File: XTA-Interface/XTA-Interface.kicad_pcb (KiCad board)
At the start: 2 copper layers, 99.9 x 99.9 mm, 19 parts, among them CN1 DRIVE 0, CN2 DRIVE 1, CN3 LEDs, CN4 Drive Power, J3 Bus_ISA_8bit, U1 BIOS FLASH, U2 74HCT245, U3 ATF/GAL16V8-15 "LEFT", U4 ATF/GAL16V8-15 "RIGHT"

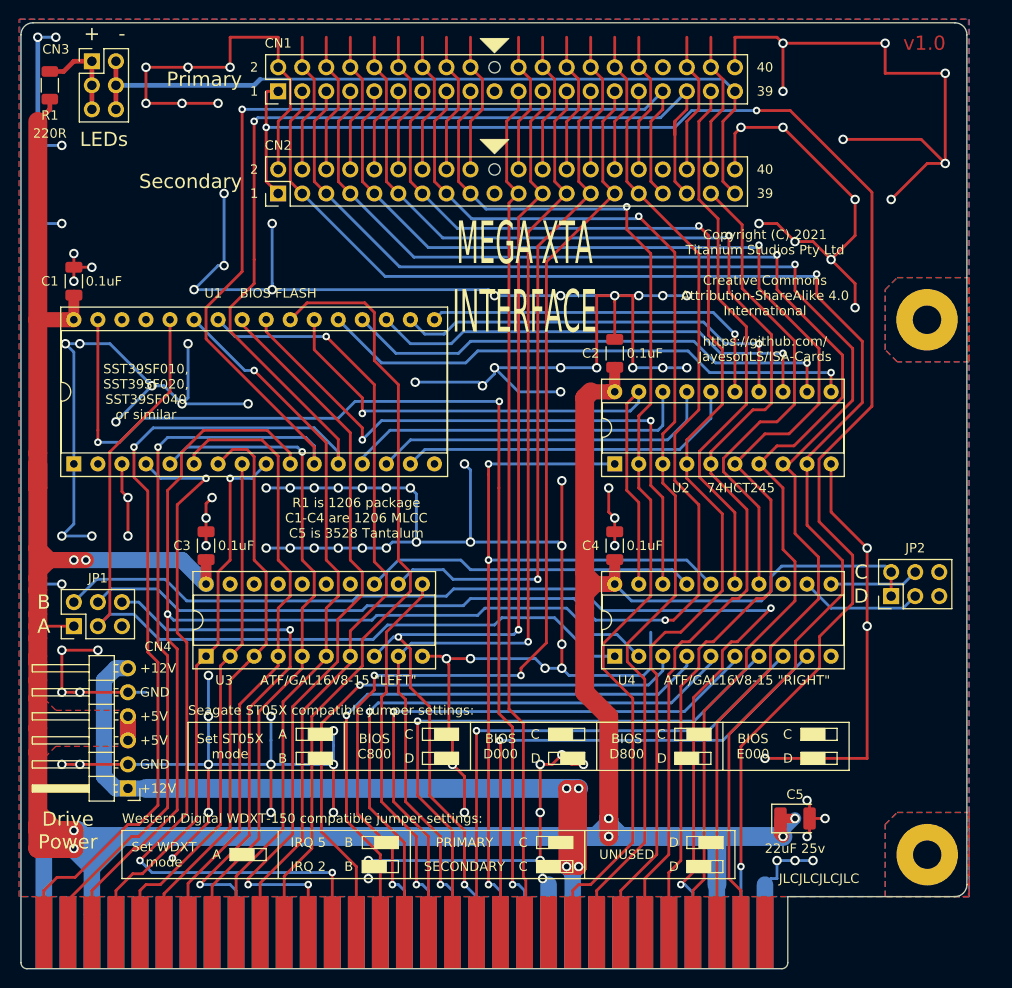
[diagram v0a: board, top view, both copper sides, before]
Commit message: Minor XTA interface tweaks.
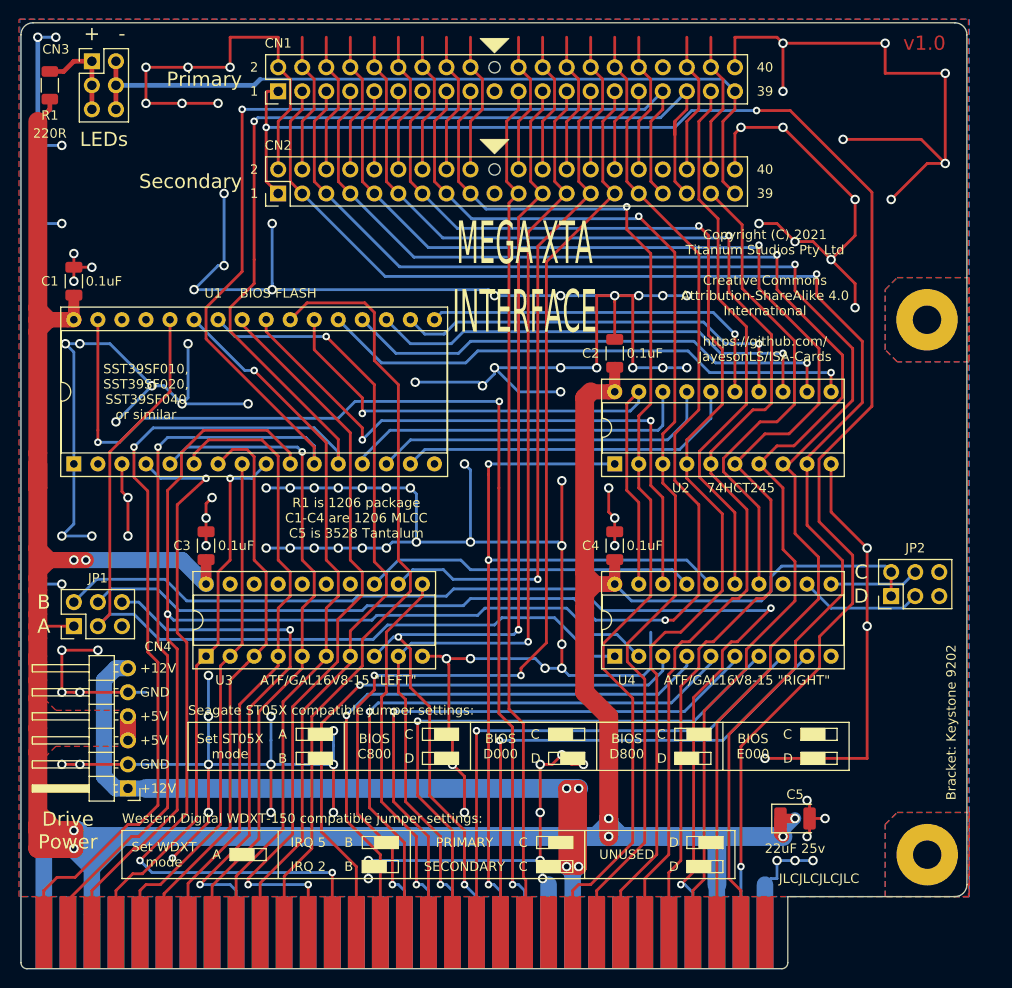
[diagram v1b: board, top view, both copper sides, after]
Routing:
- net VCC: track 367.6 -> 375.3 mm
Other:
- board text added: "Bracket: Keystone 9202"
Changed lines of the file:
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@@
   (general
     (thickness 1.6)
-    (drawings 167)
-    (tracks 1324)
+    (drawings 168)
+    (tracks 1333)
     (zones 0)
     (modules 19)
@@
     (pad 1 connect rect (at 0 0) (size 1.78 7.62) (layers B.Cu B.Mask)
       (net 28 GND))
+  )
+  (gr_text "Bracket: Keystone 9202" (at 194.945 116.205 90) (layer F.SilkS)
+    (effects (font (size 1 1) (thickness 0.15)))
   )
   (gr_text "Drive\nPower" (at 101.6 127.635) (layer F.SilkS)
@@
   (segment (start 98.806 101.854) (end 98.425 102.235) (width 0.3) (layer F.Cu) (net 29))
   (segment (start 98.425 87.757) (end 98.425 91.44) (width 2) (layer F.Cu) (net 29))
-  (segment (start 98.425 73.66) (end 98.425 87.757) (width 2) (layer F.Cu) (net 29))
   (segment (start 102.235 73.66) (end 98.425 73.66) (width 1.6) (layer F.Cu) (net 29))
   (via (at 158.75 128.27) (size 1) (drill 0.6) (layers F.Cu B.Cu) (net 29))
-  (segment (start 102.235 73.66) (end 102.235 71.071) (width 1.15) (layer F.Cu) (net 29))
   (segment (start 170.18 128.27) (end 177.165 128.27) (width 2) (layer B.Cu) (net 29))
   (via (at 177.165 128.27) (size 1) (drill 0.6) (layers F.Cu B.Cu) (net 29))
@@
   (segment (start 159.385 101.6) (end 161.163 103.378) (width 0.3) (layer B.Cu) (net 29))
   (segment (start 99.695 50.3575) (end 99.695 51.435) (width 0.5) (layer F.Cu) (net 29))
-  (segment (start 98.425 52.705) (end 98.425 73.66) (width 2) (layer F.Cu) (net 29))
   (segment (start 99.695 51.435) (end 98.425 52.705) (width 0.5) (layer F.Cu) (net 29))
   (segment (start 99.695 99.06) (end 98.425 97.79) (width 1.7) (layer F.Cu) (net 29))
@@
   (segment (start 98.425 97.79) (end 98.425 100.965) (width 2) (layer F.Cu) (net 29))
   (segment (start 98.425 100.965) (end 98.425 102.235) (width 2) (layer F.Cu) (net 29))
+  (segment (start 99.695 73.66) (end 98.425 72.39) (width 1.6) (layer F.Cu) (net 29))
+  (segment (start 98.425 72.39) (end 98.425 73.66) (width 2) (layer F.Cu) (net 29))
+  (segment (start 98.425 52.705) (end 98.425 72.39) (width 2) (layer F.Cu) (net 29))
+  (segment (start 99.695 73.66) (end 98.425 74.93) (width 1.6) (layer F.Cu) (net 29))
+  (segment (start 98.425 74.93) (end 98.425 87.757) (width 2) (layer F.Cu) (net 29))
+  (segment (start 98.425 73.66) (end 98.425 74.93) (width 2) (layer F.Cu) (net 29))
+  (segment (start 102.235 73.025) (end 101.6 73.66) (width 1.15) (layer F.Cu) (net 29))
+  (segment (start 101.6 73.66) (end 99.695 73.66) (width 1.6) (layer F.Cu) (net 29))
+  (segment (start 102.235 73.66) (end 101.6 73.66) (width 1.6) (layer F.Cu) (net 29))
+  (segment (start 102.235 72.39) (end 102.235 73.025) (width 1.15) (layer F.Cu) (net 29))
+  (segment (start 102.235 73.66) (end 102.235 72.39) (width 1.15) (layer F.Cu) (net 29))
+  (segment (start 102.235 72.39) (end 102.235 71.071) (width 1.15) (layer F.Cu) (net 29))
   (segment (start 154.305 51.435) (end 154.305 49.53) (width 0.3) (layer F.Cu) (net 30))
   (segment (start 153.044999 52.695001) (end 154.305 51.435) (width 0.3) (layer F.Cu) (net 30))

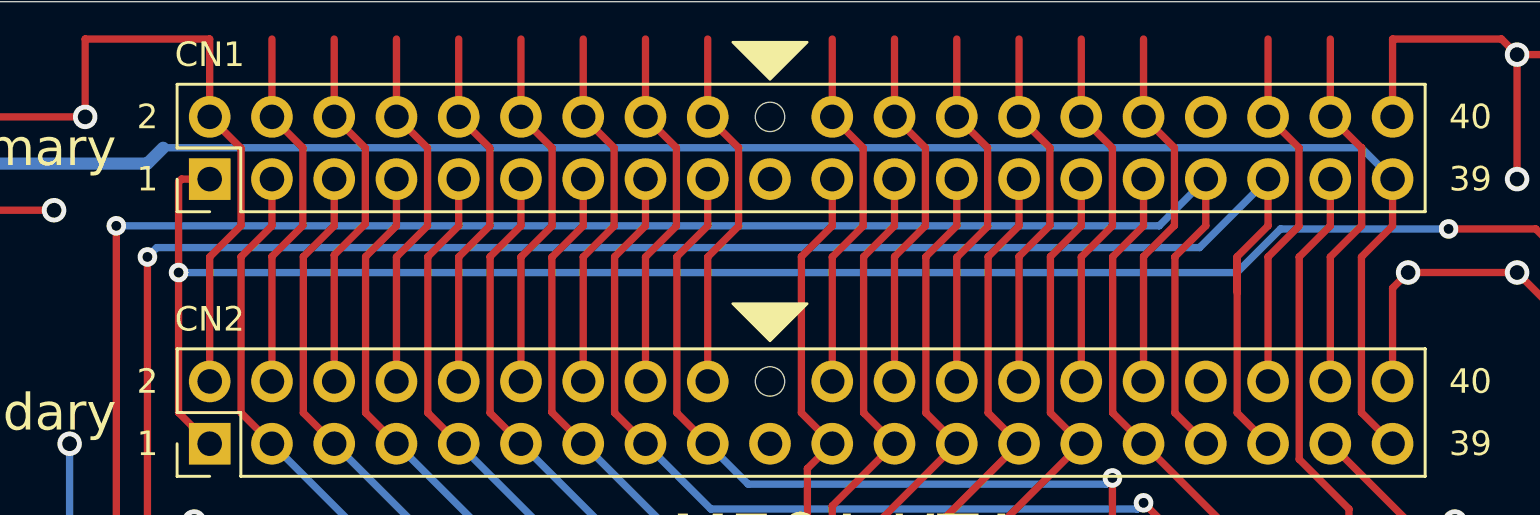
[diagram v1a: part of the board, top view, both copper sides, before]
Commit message: Add some caution messages to XTA interface.
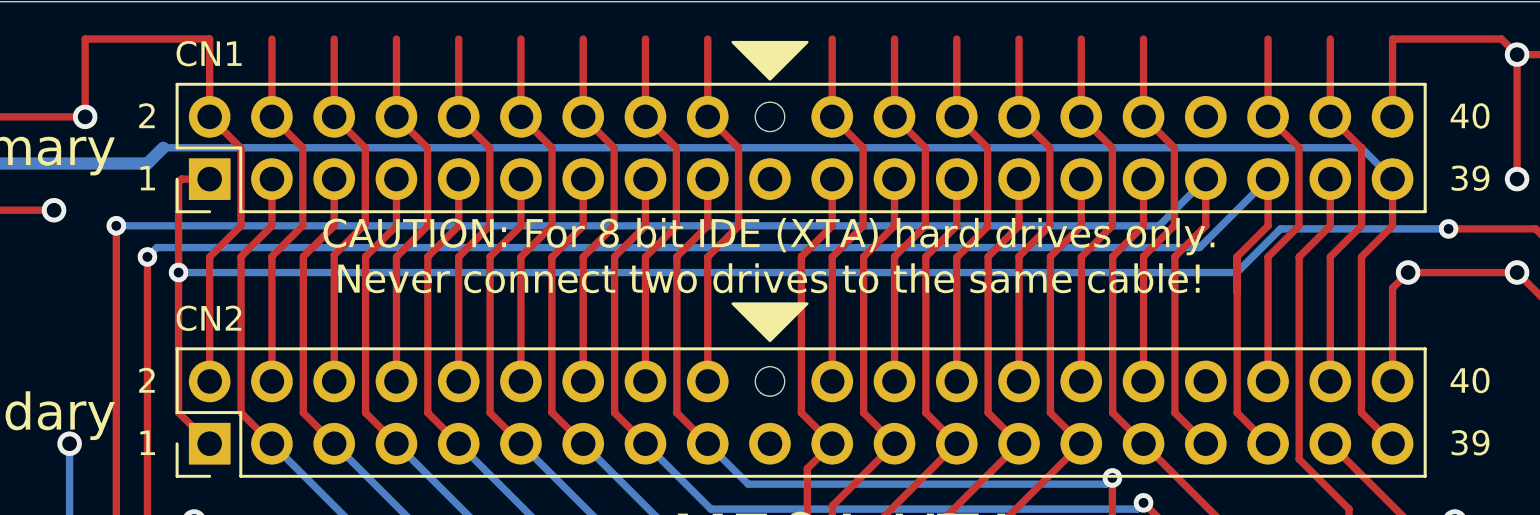
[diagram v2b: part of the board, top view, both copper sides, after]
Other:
- board text added: "CAUTION: For 8 bit IDE (XTA) hard drives only. Never connect two drives to the same cable!"

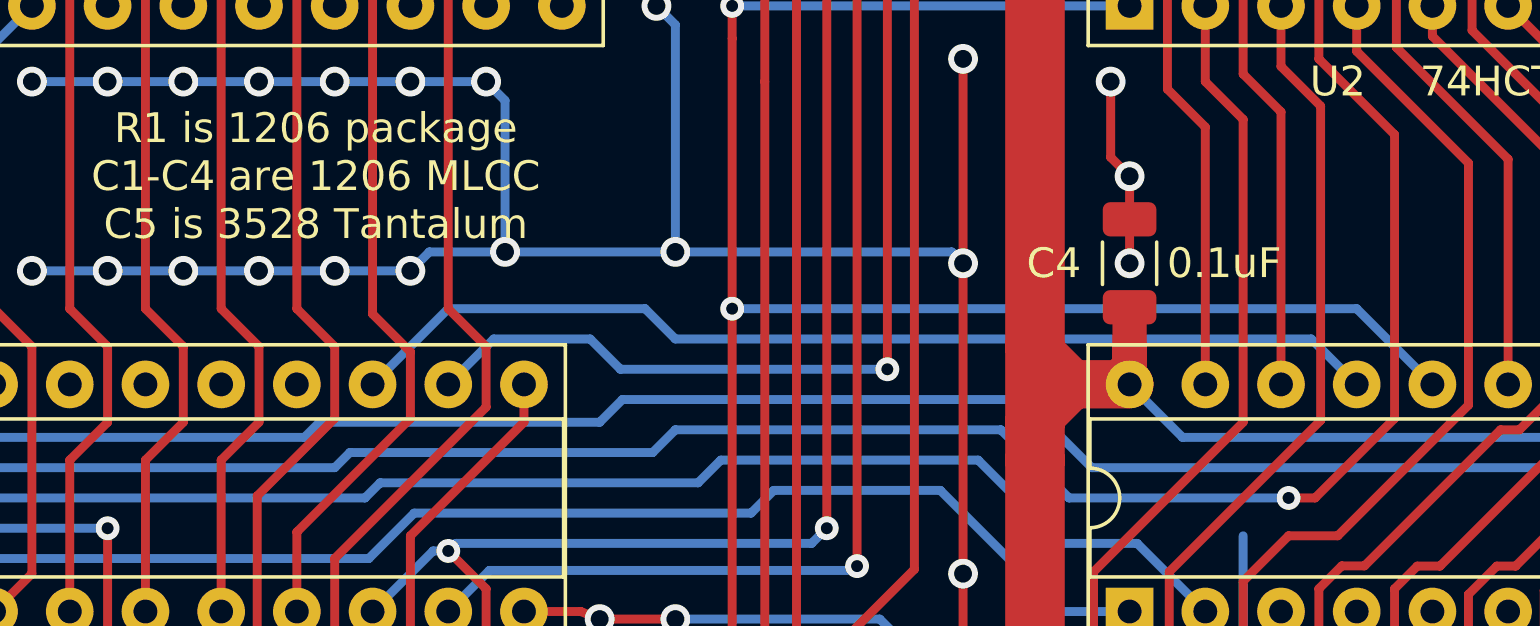
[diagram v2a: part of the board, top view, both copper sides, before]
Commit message: Add left GAL logic for XTA interface. Involved one pin swap to account for two of the 16V8 pins not having feedback.
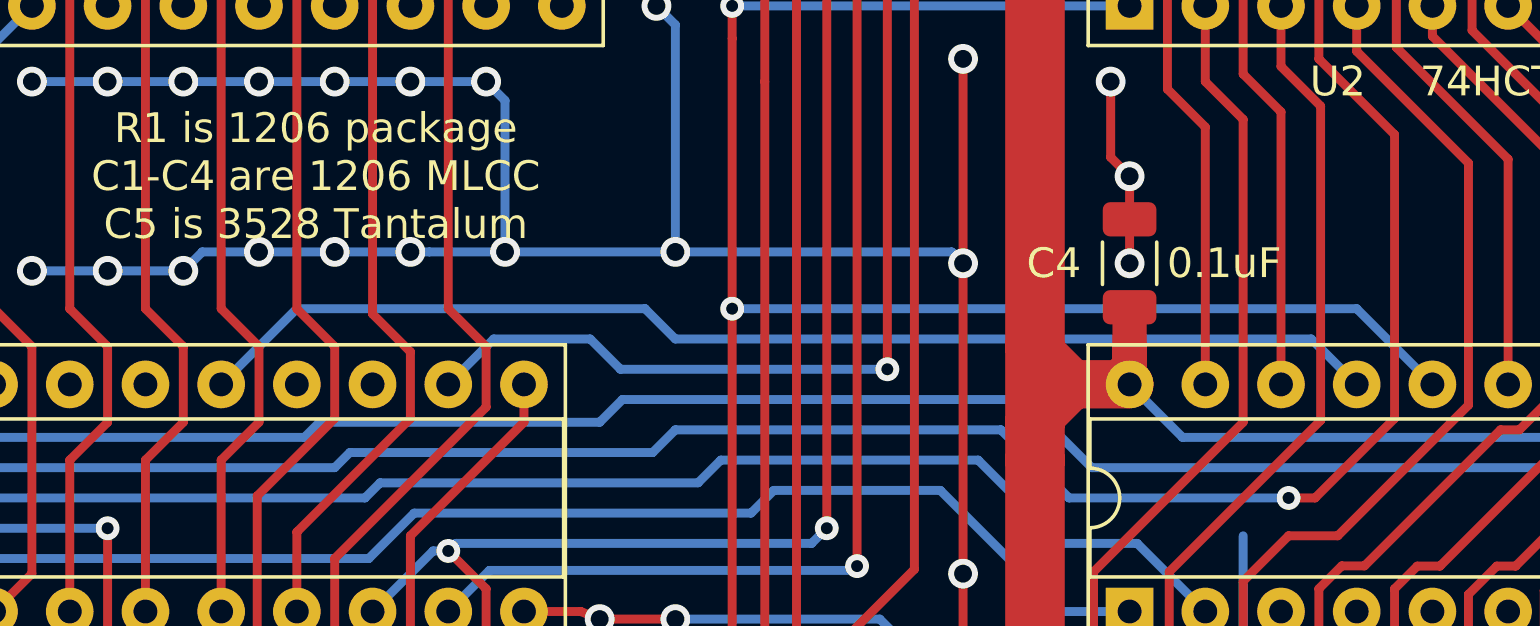
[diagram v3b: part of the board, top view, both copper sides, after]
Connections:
- net Net-(U3-Pad14) renamed /IOR_DELAY2
- net Net-(U3-Pad16) renamed /IOR_DELAY_DEBUG
- net Net-(U3-Pad17) renamed /IOR_DELAY3
- net Net-(U3-Pad18) renamed /IOR_DELAY4
- net Net-(U3-Pad19) renamed /IOR_DELAY5
- U3 pad 13: DECODE_IO_RANGE -> /IOR_DELAY1
- U3 pad 15: Net-(U3-Pad15) -> DECODE_IO_RANGE
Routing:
- net DECODE_IO_RANGE: track 35.1 -> 40.2 mm

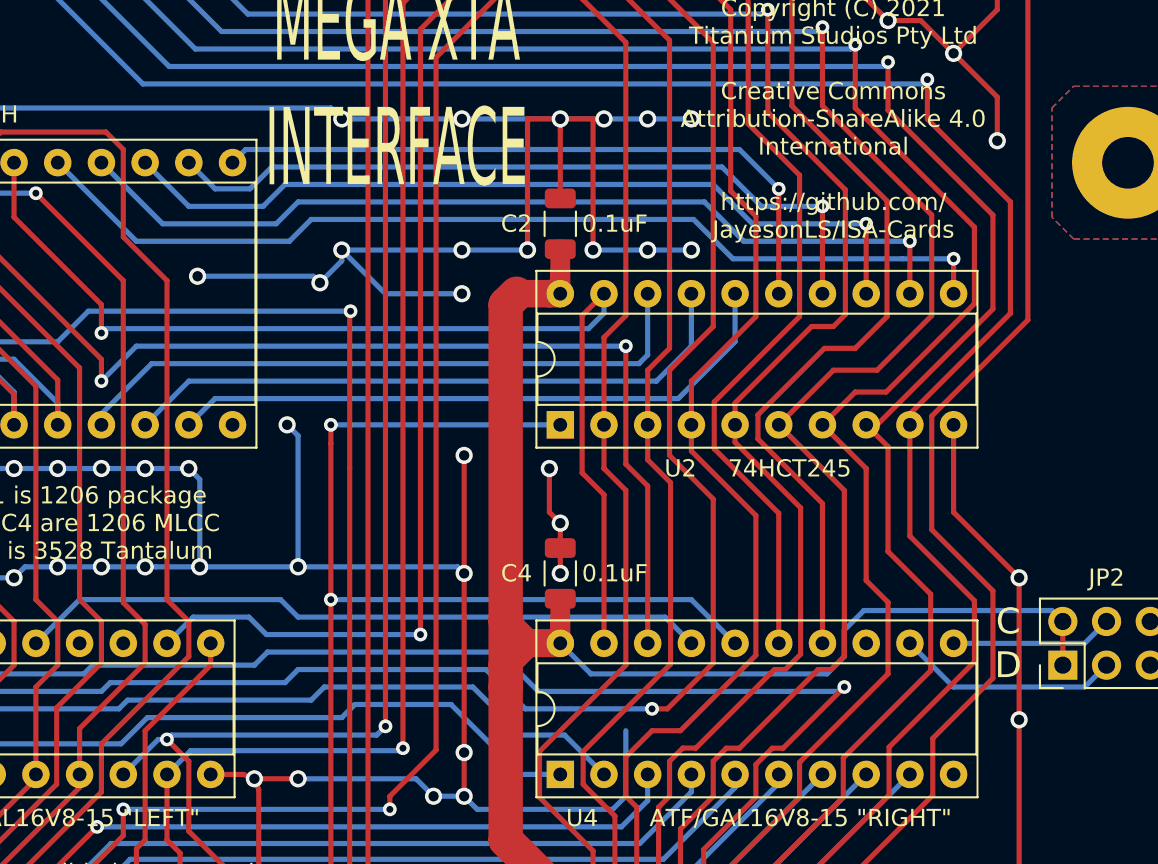
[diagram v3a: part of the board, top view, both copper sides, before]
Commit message: Add right GAL logic for XTA interface. Resulted in several circuit/board changes.
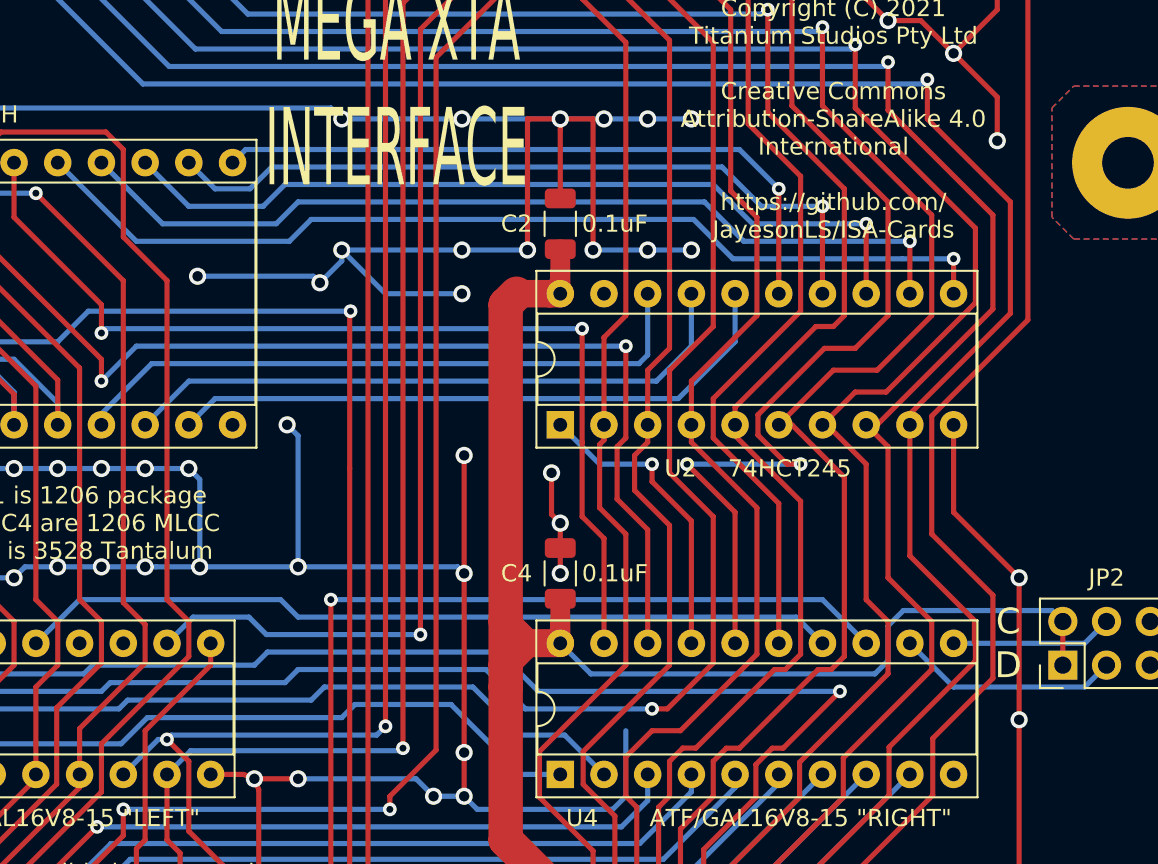
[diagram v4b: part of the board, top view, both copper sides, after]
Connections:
- U2 pad 1: ~MEMR -> BUFF_DIR
- U2 pad 19: ~CE~_BIOS -> GND
- U4 pad 13: Net-(U4-Pad13) -> ~MEMR
- U4 pad 14: ~CS_XTA1 -> DECODE_IO_RANGE
- U4 pad 16: ~MEMR -> ~CS_XTA1
- U4 pad 17: DECODE_IO_RANGE -> BUFF_DIR
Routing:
- net BUFF_DIR: track 0.00 -> 17.6 mm, vias 0 -> 1
- net ~MEMR: track 88.3 -> 72.4 mm, vias 3 -> 2
- net ~CS_XTA1: track 50.6 -> 58.4 mm, vias 0 -> 2
- net DECODE_IO_RANGE: track 40.2 -> 47.8 mm
- net ~CE~_BIOS: track 64.2 -> 58.9 mm, vias 1 -> 2
- net IRQ2: track 116.6 -> 115.8 mm
- net D1: track 116.7 -> 117.3 mm
